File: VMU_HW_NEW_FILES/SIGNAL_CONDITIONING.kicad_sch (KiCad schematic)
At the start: 78 parts, among them U1 LM358, U4 LM358, U5 LM358, U6 LM358

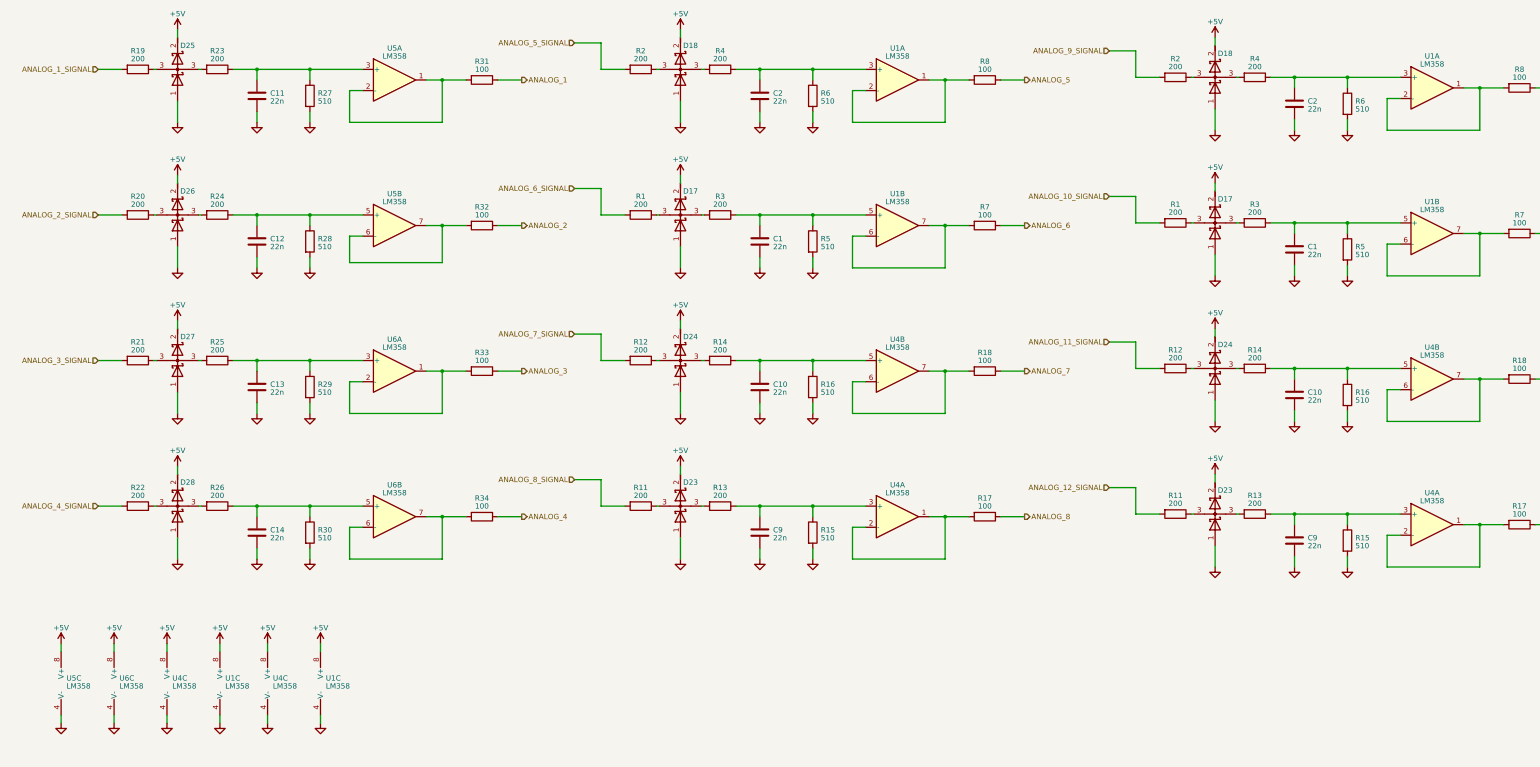
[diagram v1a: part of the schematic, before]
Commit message: tog bort fel signal fil
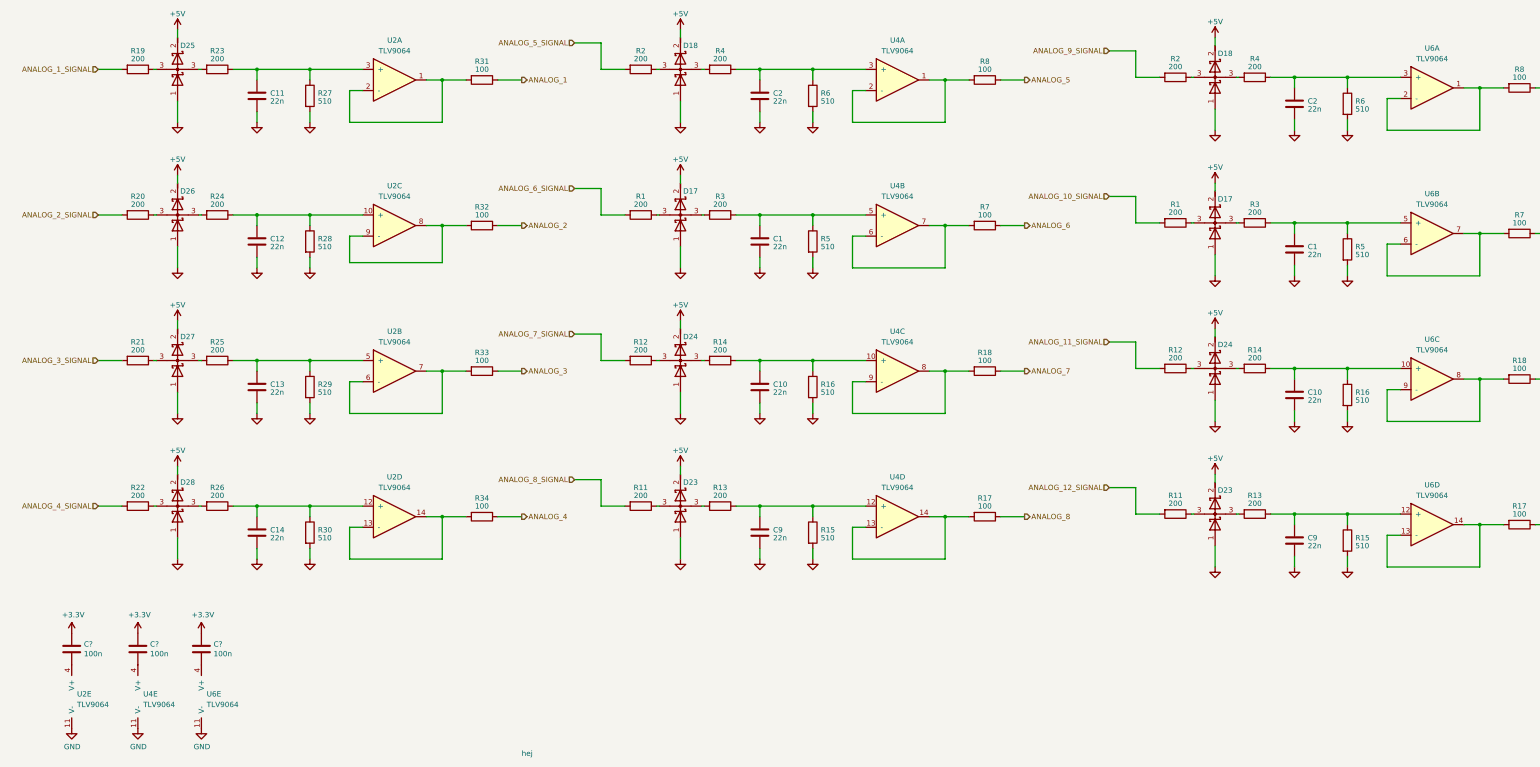
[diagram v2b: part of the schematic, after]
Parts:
- removed U1 (x2), U4 (x2), U5, U6: LM358, Package_SO:SOIC-8_3.9x4.9mm_P1.27mm, symbol Amplifier_Operational:LM358
- added C? (x3): 100n, Capacitor_SMD:C_0603_1608Metric, symbol Device:C
- added U2, U4, U6: TLV9064, Package_SO:SOIC-14_3.9x8.7mm_P1.27mm, symbol KTHFS:TLV9064
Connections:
- net GND: now also U2.11 (V-), U4.11 (V-), U6.11 (V-)
- net at C11.1, R23.1, R27.1: now also U2.3 (+)
- net at R31.2: now also U2.1, U2.2 (-)
- net at C12.1, R24.1, R28.1: now also U2.10 (+)
- net at R32.2: now also U2.8, U2.9 (-)
- net at C13.1, R25.1, R29.1: now also U2.5 (+)
- net at R33.2: now also U2.6 (-), U2.7
- net at C14.1, R26.1, R30.1: now also U2.12 (+)
- net at R34.2: now also U2.13 (-), U2.14
- net at C1.1, R3.1, R5.1: now also U4.5 (+)
- net at R7.2: now also U4.6 (-), U4.7
- net at R8.2: now also U4.1, U4.2 (-)
- net at C2.1, R4.1, R6.1: now also U4.3 (+)
- net at C10.1, R14.1, R16.1: now also U4.10 (+)
- net at R18.2: now also U4.8, U4.9 (-)
- net at C9.1, R13.1, R15.1: now also U4.12 (+)
- net at R17.2: now also U4.13 (-), U4.14
- net at C1.1, R3.1, R5.1: now also U6.5 (+)
- net at C2.1, R4.1, R6.1: now also U6.3 (+)
- net at R17.2: now also U6.13 (-), U6.14
- net at C10.1, R14.1, R16.1: now also U6.10 (+)
- net at R18.2: now also U6.8, U6.9 (-)
- net at R7.2: now also U6.6 (-), U6.7
- net at R8.2: now also U6.1, U6.2 (-)
- net at C9.1, R13.1, R15.1: now also U6.12 (+)
- new net: C?.2, U6.4 (V+)
- new net: C?.2, U4.4 (V+)
- new net: C?.2, U2.4 (V+)
- new net +3V3: C?.1, C?.1, C?.1
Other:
- note added: "hej"
